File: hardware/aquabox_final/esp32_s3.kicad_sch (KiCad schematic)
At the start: 0 parts

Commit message: Atualização
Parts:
- added U2: ESP32-S3-DEVKITC-1-N16R8V, ESP32-S3-DEVKITC-1-N16R8V:XCVR_ESP32-S3-DEVKITC-1-N16R8V, symbol ESP32-S3-DEVKITC-1-N16R8V:ESP32-S3-DEVKITC-1-N16R8V
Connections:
- new net 3V3: U2.J1_1 (3V3), U2.J1_2 (3V3)
- new net GND: U2.J1_22 (GND), U2.J3_1 (GND), U2.J3_21 (GND), U2.J3_22 (GND)

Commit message: Atualização
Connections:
- net SOL_1: now reaches U2.J1_10 (GPIO17)
- net SOL_2: now reaches U2.J1_11 (GPIO18)
- net TFT_DC: now reaches U2.J1_12 (GPIO8)
- net TFT_CS: now reaches U2.J1_15 (GPIO9)
- net TFT_RST: now reaches U2.J1_16 (GPIO10)
- net SPI_MOSI: now reaches U2.J1_17 (GPIO11)
- net SPI_SCK: now reaches U2.J1_18 (GPIO12)
- net SD_CS: now reaches U2.J1_19 (GPIO13)
- net FLOW_SENSOR: now reaches U2.J1_20 (GPIO14)
- net BTN_UP: now reaches U2.J1_4 (GPIO4)
- net BTN_DOWN: now reaches U2.J1_5 (GPIO5)
- net BTN_ENTER: now reaches U2.J1_6 (GPIO6)
- net TFT_BL: now reaches U2.J1_7 (GPIO7)
- net BTN_BACK: now reaches U2.J1_8 (GPIO15)
- net RELAY_PUMP: now reaches U2.J1_9 (GPIO16)
- net SOL_3: now reaches U2.J3_18 (GPIO21)
- net LEVEL_LOW_3: now reaches U2.J3_2 (U0TXD/GPIO43)
- net LEVEL_HIGH_3: now reaches U2.J3_3 (U0RXD/GPIO44)
- net I2C_SDA: now reaches U2.J3_4 (GPIO1)
- net I2C_SCL: now reaches U2.J3_5 (GPIO2)
- net LEVEL_HIGH_2: now reaches U2.J3_6 (MTMS/GPIO42)
- net LEVEL_LOW_2: now reaches U2.J3_7 (MTDI/GPIO41)
- net LEVEL_HIGH_1: now reaches U2.J3_8 (MTDO/GPIO40)
- net LEVEL_LOW_1: now reaches U2.J3_9 (MTCK/GPIO39)
- net 3V3 renamed +3.3V
- no-connect marks 0 -> 13
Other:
- moved on the sheet: U2

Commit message: Atualização
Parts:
- added J7: TFT 1.8{dblquote}, 5104338-1:TE_5104338-1, symbol 5104338-1:5104338-1
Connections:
- net +3.3V: now also J7.1
- net GND: now also J7.10
- net SD_CS: now also J7.8
- net SPI_MOSI: now also J7.6
- net SPI_SCK: now also J7.7
- net TFT_BL: now also J7.2
- net TFT_CS: now also J7.4
- net TFT_DC: now also J7.3
- net TFT_RST: now also J7.5
- net FLOW_SENSOR renamed FLOW_COUNTER
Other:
- company: (none) -> INVENCTUS Soluções Tecnológicas
- title: (none) -> ESP32_S3
- moved on the sheet: U2

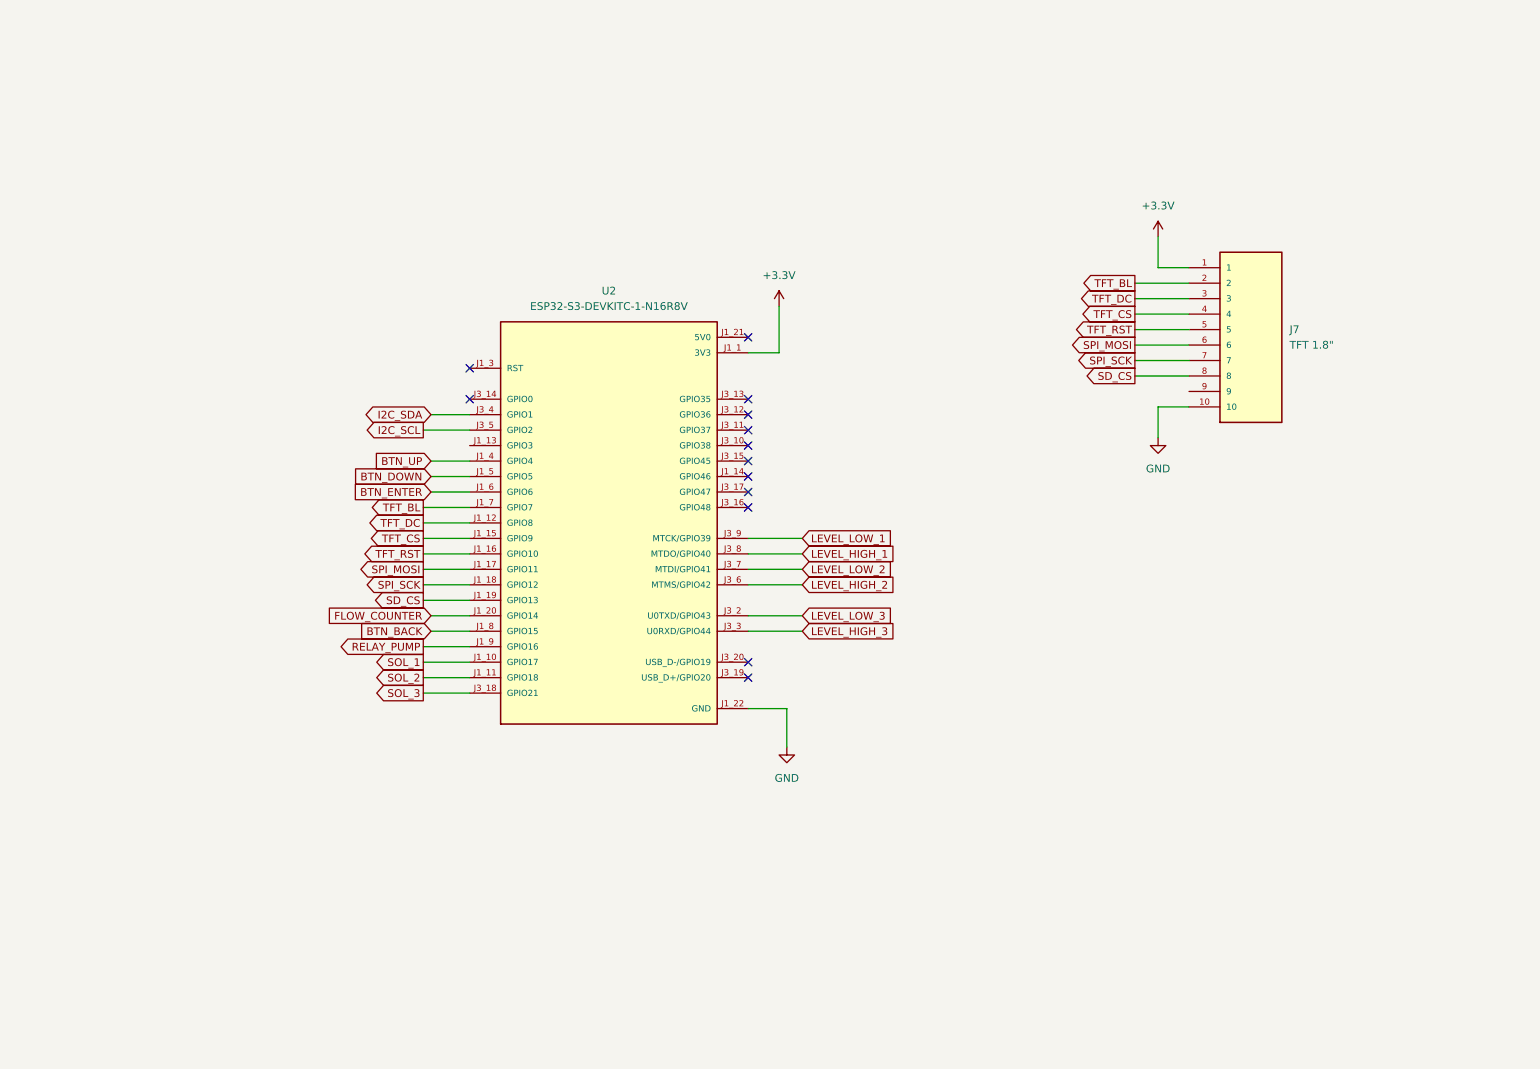
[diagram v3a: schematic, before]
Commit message: Conector do display e teclado
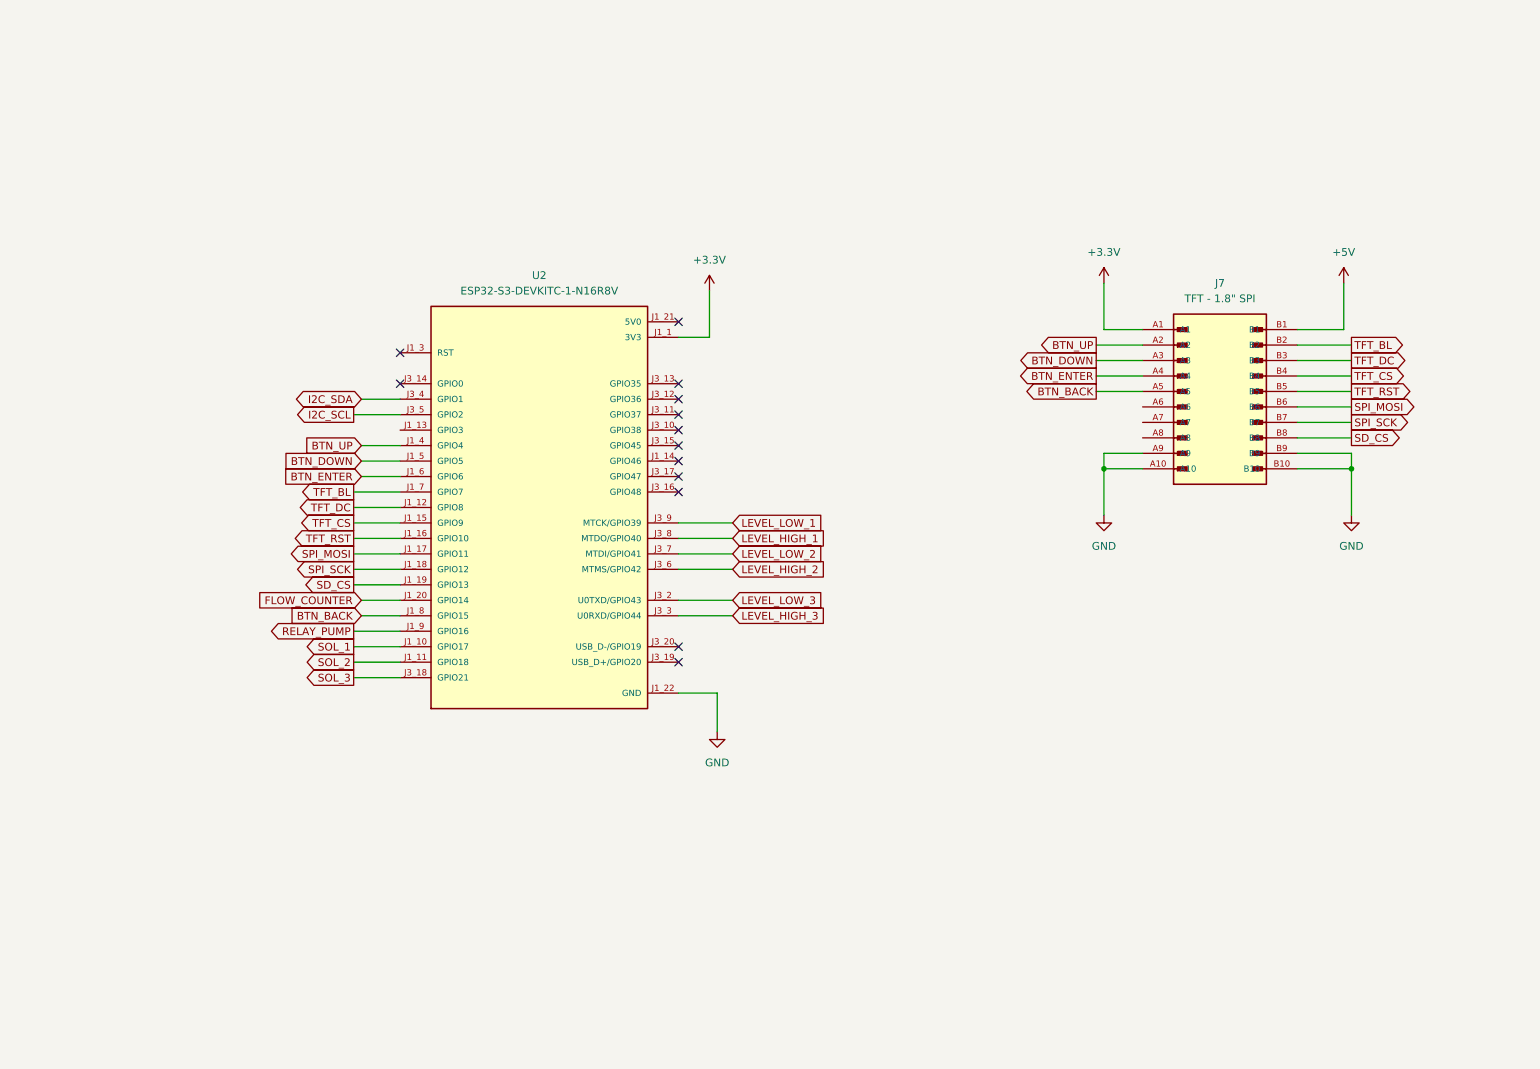
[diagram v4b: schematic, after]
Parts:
- removed J7: TFT 1.8{dblquote}, 5104338-1:TE_5104338-1, symbol 5104338-1:5104338-1
- added J7: TFT - 1.8{dblquote} SPI, 68664-008LF:AMPHENOL_68664-008LF, symbol Conect_2x10:68664-008LF
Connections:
- net +3.3V: now also J7.A1
- net BTN_BACK: now also J7.A5
- net BTN_DOWN: now also J7.A3
- net BTN_ENTER: now also J7.A4
- net BTN_UP: now also J7.A2
- net GND: now also J7.A10, J7.A9, J7.B10, J7.B9
- net SD_CS: now also J7.B8
- net SPI_MOSI: now also J7.B6
- net SPI_SCK: now also J7.B7
- net TFT_BL: now also J7.B2
- net TFT_CS: now also J7.B4
- net TFT_DC: now also J7.B3
- net TFT_RST: now also J7.B5
- new net +5V: J7.B1
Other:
- moved on the sheet: U2

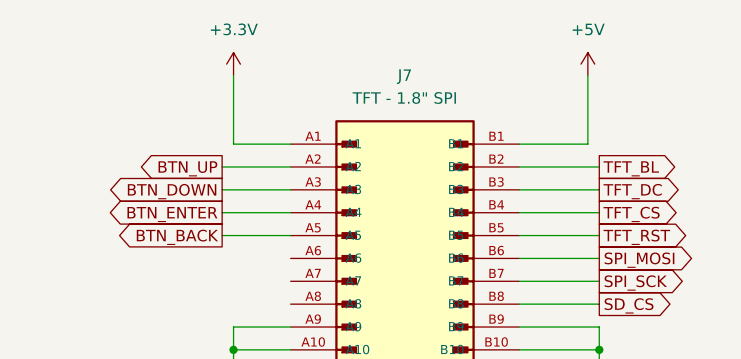
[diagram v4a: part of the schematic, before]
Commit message: Acionamento da bom e solenóides
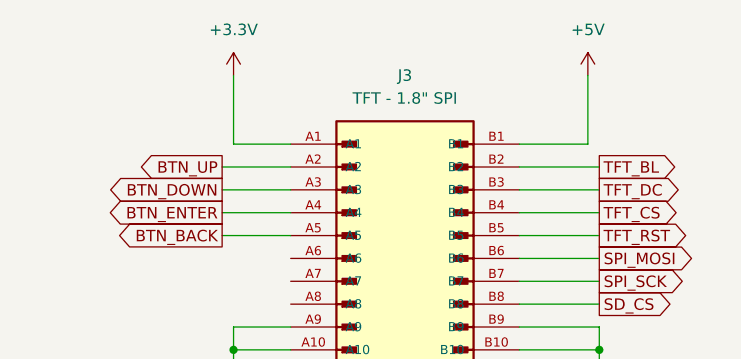
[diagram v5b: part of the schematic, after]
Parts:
- renumbered J7 to J3
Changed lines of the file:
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@@
 		(dnp no)
 		(fields_autoplaced yes)
-		(property "Reference" "#PWR06"
+		(property "Reference" "#PWR08"
 			(at 142.24 66.04 0)
 			(hide yes)
@@
 			(project "aquabox_final"
 				(path "/c895ac8d-c639-4fea-ba83-739985d9c75e/38445a07-7dc1-4dfd-aa58-185ce46ba2bf"
-					(reference "#PWR06")
+					(reference "#PWR08")
 					(unit 1)
 				)
@@
 		(dnp no)
 		(fields_autoplaced yes)
-		(property "Reference" "#PWR039"
+		(property "Reference" "#PWR013"
 			(at 247.65 105.41 0)
 			(hide yes)
@@
 			(project "aquabox_final"
 				(path "/c895ac8d-c639-4fea-ba83-739985d9c75e/38445a07-7dc1-4dfd-aa58-185ce46ba2bf"
-					(reference "#PWR039")
+					(reference "#PWR013")
 					(unit 1)
 				)
@@
 		(dnp no)
 		(fields_autoplaced yes)
-		(property "Reference" "#PWR026"
+		(property "Reference" "#PWR012"
 			(at 246.38 64.77 0)
 			(hide yes)
@@
 			(project "aquabox_final"
 				(path "/c895ac8d-c639-4fea-ba83-739985d9c75e/38445a07-7dc1-4dfd-aa58-185ce46ba2bf"
-					(reference "#PWR026")
+					(reference "#PWR012")
 					(unit 1)
 				)
@@
 		(dnp no)
 		(fields_autoplaced yes)
-		(property "Reference" "#PWR037"
+		(property "Reference" "#PWR010"
 			(at 207.01 64.77 0)
 			(hide yes)
@@
 			(project "aquabox_final"
 				(path "/c895ac8d-c639-4fea-ba83-739985d9c75e/38445a07-7dc1-4dfd-aa58-185ce46ba2bf"
-					(reference "#PWR037")
+					(reference "#PWR010")
 					(unit 1)
 				)
@@
 		(dnp no)
 		(fields_autoplaced yes)
-		(property "Reference" "#PWR07"
+		(property "Reference" "#PWR09"
 			(at 143.51 140.97 0)
 			(hide yes)
@@
 			(project "aquabox_final"
 				(path "/c895ac8d-c639-4fea-ba83-739985d9c75e/38445a07-7dc1-4dfd-aa58-185ce46ba2bf"
-					(reference "#PWR07")
+					(reference "#PWR09")
 					(unit 1)
 				)
@@
 		(dnp no)
 		(fields_autoplaced yes)
-		(property "Reference" "#PWR038"
+		(property "Reference" "#PWR011"
 			(at 207.01 105.41 0)
 			(hide yes)
@@
 			(project "aquabox_final"
 				(path "/c895ac8d-c639-4fea-ba83-739985d9c75e/38445a07-7dc1-4dfd-aa58-185ce46ba2bf"
-					(reference "#PWR038")
+					(reference "#PWR011")
 					(unit 1)
 				)
@@
 		(dnp no)
 		(fields_autoplaced yes)
-		(property "Reference" "J7"
+		(property "Reference" "J3"
 			(at 226.06 60.96 0)
 			(show_name no)
@@
 			(project "aquabox_final"
 				(path "/c895ac8d-c639-4fea-ba83-739985d9c75e/38445a07-7dc1-4dfd-aa58-185ce46ba2bf"
-					(reference "J7")
+					(reference "J3")
 					(unit 1)
 				)

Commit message: Atualização
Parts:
- added C3, C4, C5, C6, C7, C8: 100n, symbol Device:C
- added R12, R43, R44, R5, R8, R9: 10K, symbol Device:R
- added SW1: MANUAL?AUTOMATICO, symbol Switch:SW_SPST
- added SW2: BOMBA, symbol Switch:SW_SPST
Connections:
- net +3.3V: now also R12.1, R43.1, R44.1, R5.1, R8.1, R9.1
- net BTN_BACK: now also C6.1, R12.2
- net BTN_DOWN: now also C4.1, R8.2
- net BTN_ENTER: now also C5.1, R9.2
- net BTN_UP: now also C3.1, R5.2
- net GND: now also C3.2, C4.2, C5.2, C6.2, C7.2, C8.2, SW1.1 (A), SW2.1 (A)
- net BOMBA_ON_OFF: now reaches U2.J3_10 (GPIO38)
- net BOMBA_ON_OFF: now also C7.1, R44.2, SW1.2 (B)
- net MAN_AUTO: now reaches U2.J3_17 (GPIO47)
- net MAN_AUTO: now also C8.1, R43.2, SW2.2 (B)
- no-connect marks 13 -> 12
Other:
- moved on the sheet: J3, U2

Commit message: Implementação do RTC
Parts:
- renumbered C7 to C6, C6 to C7, R5 to R4, R8 to R5, R9 to R6, R44 to R7, R12 to R8, R43 to R9, SW2 to SW1, SW1 to SW2
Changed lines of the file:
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@@
 		(dnp no)
 		(fields_autoplaced yes)
-		(property "Reference" "#PWR08"
+		(property "Reference" "#PWR013"
 			(at 172.72 67.31 0)
 			(hide yes)
@@
 			(project "aquabox_final"
 				(path "/c895ac8d-c639-4fea-ba83-739985d9c75e/38445a07-7dc1-4dfd-aa58-185ce46ba2bf"
-					(reference "#PWR08")
+					(reference "#PWR013")
 					(unit 1)
 				)
@@
 		(dnp no)
 		(fields_autoplaced yes)
-		(property "Reference" "#PWR065"
+		(property "Reference" "#PWR012"
 			(at 66.04 67.31 0)
 			(hide yes)
@@
 			(project "aquabox_final"
 				(path "/c895ac8d-c639-4fea-ba83-739985d9c75e/38445a07-7dc1-4dfd-aa58-185ce46ba2bf"
-					(reference "#PWR065")
+					(reference "#PWR012")
 					(unit 1)
 				)
@@
 		(dnp no)
 		(fields_autoplaced yes)
-		(property "Reference" "R43"
+		(property "Reference" "R9"
 			(at 68.58 31.7499 0)
 			(show_name no)
@@
 			(project "aquabox_final"
 				(path "/c895ac8d-c639-4fea-ba83-739985d9c75e/38445a07-7dc1-4dfd-aa58-185ce46ba2bf"
-					(reference "R43")
+					(reference "R9")
 					(unit 1)
 				)
@@
 		(dnp no)
 		(fields_autoplaced yes)
-		(property "Reference" "R44"
+		(property "Reference" "R7"
 			(at 55.88 31.7499 0)
 			(show_name no)
@@
 			(project "aquabox_final"
 				(path "/c895ac8d-c639-4fea-ba83-739985d9c75e/38445a07-7dc1-4dfd-aa58-185ce46ba2bf"
-					(reference "R44")
+					(reference "R7")
 					(unit 1)
 				)
@@
 		(dnp no)
 		(fields_autoplaced yes)
-		(property "Reference" "R5"
+		(property "Reference" "R4"
 			(at 33.02 149.8599 0)
 			(show_name no)
@@
 			(project "aquabox_final"
 				(path "/c895ac8d-c639-4fea-ba83-739985d9c75e/38445a07-7dc1-4dfd-aa58-185ce46ba2bf"
-					(reference "R5")
+					(reference "R4")
 					(unit 1)
 				)
@@
 		(dnp no)
 		(fields_autoplaced yes)
-		(property "Reference" "#PWR013"
+		(property "Reference" "#PWR018"
 			(at 262.89 88.9 0)
 			(hide yes)
@@
 			(project "aquabox_final"
 				(path "/c895ac8d-c639-4fea-ba83-739985d9c75e/38445a07-7dc1-4dfd-aa58-185ce46ba2bf"
-					(reference "#PWR013")
+					(reference "#PWR018")
 					(unit 1)
 				)
@@
 		(dnp no)
 		(fields_autoplaced yes)
-		(property "Reference" "SW2"
+		(property "Reference" "SW1"
 			(at 38.1 41.91 0)
 			(show_name no)
@@
 			(project "aquabox_final"
 				(path "/c895ac8d-c639-4fea-ba83-739985d9c75e/38445a07-7dc1-4dfd-aa58-185ce46ba2bf"
-					(reference "SW2")
+					(reference "SW1")
 					(unit 1)
 				)
@@
 		(dnp no)
 		(fields_autoplaced yes)
-		(property "Reference" "#PWR020"
+		(property "Reference" "#PWR010"
 			(at 58.42 146.05 0)
 			(hide yes)
@@
 			(project "aquabox_final"
 				(path "/c895ac8d-c639-4fea-ba83-739985d9c75e/38445a07-7dc1-4dfd-aa58-185ce46ba2bf"
-					(reference "#PWR020")
+					(reference "#PWR010")
 					(unit 1)
 				)
@@
 		(dnp no)
 		(fields_autoplaced yes)
-		(property "Reference" "R12"
+		(property "Reference" "R8"
 			(at 60.96 149.8599 0)
 			(show_name no)
@@
 			(project "aquabox_final"
 				(path "/c895ac8d-c639-4fea-ba83-739985d9c75e/38445a07-7dc1-4dfd-aa58-185ce46ba2bf"
-					(reference "R12")
+					(reference "R8")
 					(unit 1)
 				)
@@
 		(dnp no)
 		(fields_autoplaced yes)
-		(property "Reference" "R8"
+		(property "Reference" "R5"
 			(at 41.91 149.8599 0)
 			(show_name no)
@@
 			(project "aquabox_final"
 				(path "/c895ac8d-c639-4fea-ba83-739985d9c75e/38445a07-7dc1-4dfd-aa58-185ce46ba2bf"
-					(reference "R8")
+					(reference "R5")
 					(unit 1)
 				)
@@
 		(dnp no)
 		(fields_autoplaced yes)
-		(property "Reference" "SW1"
+		(property "Reference" "SW2"
 			(at 39.37 31.75 0)
 			(show_name no)
@@
 			(project "aquabox_final"
 				(path "/c895ac8d-c639-4fea-ba83-739985d9c75e/38445a07-7dc1-4dfd-aa58-185ce46ba2bf"
-					(reference "SW1")
+					(reference "SW2")
 					(unit 1)
 				)
@@
 		(dnp no)
 		(fields_autoplaced yes)
-		(property "Reference" "#PWR066"
+		(property "Reference" "#PWR09"
 			(at 53.34 26.67 0)
 			(hide yes)
@@
 			(project "aquabox_final"
 				(path "/c895ac8d-c639-4fea-ba83-739985d9c75e/38445a07-7dc1-4dfd-aa58-185ce46ba2bf"
-					(reference "#PWR066")
+					(reference "#PWR09")
 					(unit 1)
 				)
@@
 		(dnp no)
 		(fields_autoplaced yes)
-		(property "Reference" "#PWR012"
+		(property "Reference" "#PWR017"
 			(at 261.62 48.26 0)
 			(hide yes)
@@
 			(project "aquabox_final"
 				(path "/c895ac8d-c639-4fea-ba83-739985d9c75e/38445a07-7dc1-4dfd-aa58-185ce46ba2bf"
-					(reference "#PWR012")
+					(reference "#PWR017")
 					(unit 1)
 				)
@@
 		(dnp no)
 		(fields_autoplaced yes)
-		(property "Reference" "C6"
+		(property "Reference" "C7"
 			(at 62.23 171.4499 0)
 			(show_name no)
@@
 			(project "aquabox_final"
 				(path "/c895ac8d-c639-4fea-ba83-739985d9c75e/38445a07-7dc1-4dfd-aa58-185ce46ba2bf"
-					(reference "C6")
+					(reference "C7")
 					(unit 1)
 				)
@@
 		(dnp no)
 		(fields_autoplaced yes)
-		(property "Reference" "#PWR010"
+		(property "Reference" "#PWR015"
 			(at 222.25 48.26 0)
 			(hide yes)
@@
 			(project "aquabox_final"
 				(path "/c895ac8d-c639-4fea-ba83-739985d9c75e/38445a07-7dc1-4dfd-aa58-185ce46ba2bf"
-					(reference "#PWR010")
+					(reference "#PWR015")
 					(unit 1)
 				)
@@
 		(dnp no)
 		(fields_autoplaced yes)
-		(property "Reference" "R9"
+		(property "Reference" "R6"
 			(at 50.8 149.8599 0)
 			(show_name no)
@@
 			(project "aquabox_final"
 				(path "/c895ac8d-c639-4fea-ba83-739985d9c75e/38445a07-7dc1-4dfd-aa58-185ce46ba2bf"
-					(reference "R9")
+					(reference "R6")
 					(unit 1)
 				)
@@
 		(dnp no)
 		(fields_autoplaced yes)
-		(property "Reference" "#PWR067"
+		(property "Reference" "#PWR08"
 			(at 30.48 67.31 0)
 			(hide yes)
@@
 			(project "aquabox_final"
 				(path "/c895ac8d-c639-4fea-ba83-739985d9c75e/38445a07-7dc1-4dfd-aa58-185ce46ba2bf"
-					(reference "#PWR067")
+					(reference "#PWR08")
 					(unit 1)
 				)
@@
 		(dnp no)
 		(fields_autoplaced yes)
-		(property "Reference" "#PWR09"
+		(property "Reference" "#PWR014"
 			(at 173.99 142.24 0)
 			(hide yes)
@@
 			(project "aquabox_final"
 				(path "/c895ac8d-c639-4fea-ba83-739985d9c75e/38445a07-7dc1-4dfd-aa58-185ce46ba2bf"
-					(reference "#PWR09")
+					(reference "#PWR014")
 					(unit 1)
 				)
@@
 		(dnp no)
 		(fields_autoplaced yes)
-		(property "Reference" "#PWR021"
+		(property "Reference" "#PWR011"
 			(at 58.42 187.96 0)
 			(hide yes)
@@
 			(project "aquabox_final"
 				(path "/c895ac8d-c639-4fea-ba83-739985d9c75e/38445a07-7dc1-4dfd-aa58-185ce46ba2bf"
-					(reference "#PWR021")
+					(reference "#PWR011")
 					(unit 1)
 				)
@@
 		(dnp no)
 		(fields_autoplaced yes)
-		(property "Reference" "C7"
+		(property "Reference" "C6"
 			(at 57.15 53.3399 0)
 			(show_name no)
@@
 			(project "aquabox_final"
 				(path "/c895ac8d-c639-4fea-ba83-739985d9c75e/38445a07-7dc1-4dfd-aa58-185ce46ba2bf"
-					(reference "C7")
+					(reference "C6")
 					(unit 1)
 				)
@@
 		(dnp no)
 		(fields_autoplaced yes)
-		(property "Reference" "#PWR011"
+		(property "Reference" "#PWR016"
 			(at 222.25 88.9 0)
 			(hide yes)
@@
 			(project "aquabox_final"
 				(path "/c895ac8d-c639-4fea-ba83-739985d9c75e/38445a07-7dc1-4dfd-aa58-185ce46ba2bf"
-					(reference "#PWR011")
-					(unit 1)
-				)
+					(reference "#PWR016")
+					(unit 1)
+				)

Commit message: Atualização
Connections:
- net LEVEL_HIGH_1 renamed T1_HIGH
- net LEVEL_HIGH_2 renamed T2_HIGH
- net LEVEL_HIGH_3 renamed T3_HIGH
- net LEVEL_LOW_1 renamed T1_LOW
- net LEVEL_LOW_2 renamed T2_LOW
- net LEVEL_LOW_3 renamed T3_LOW
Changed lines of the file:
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@@
 		)
 	)
-	(global_label "LEVEL_HIGH_3"
+	(global_label "T3_HIGH"
 		(shape input)
 		(at 176.53 116.84 0)
@@
 		)
 	)
-	(global_label "LEVEL_LOW_2"
+	(global_label "T2_LOW"
 		(shape input)
 		(at 176.53 106.68 0)
@@
 		)
 	)
-	(global_label "LEVEL_HIGH_1"
+	(global_label "T1_HIGH"
 		(shape input)
 		(at 176.53 104.14 0)
@@
 		)
 	)
-	(global_label "LEVEL_LOW_1"
+	(global_label "T1_LOW"
 		(shape input)
 		(at 176.53 101.6 0)
@@
 		)
 	)
-	(global_label "LEVEL_HIGH_2"
+	(global_label "T2_HIGH"
 		(shape input)
 		(at 176.53 109.22 0)
@@
 		)
 	)
-	(global_label "LEVEL_LOW_3"
+	(global_label "T3_LOW"
 		(shape input)
 		(at 176.53 114.3 0)
